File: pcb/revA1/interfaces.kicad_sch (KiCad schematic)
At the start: 18 parts, among them J2 Conn_02x30_Row_Letter_First, SW1 SW_DIP_x05, U22 SN74LV1T34DBV, U3 74AHCT1G125DB, U4 SN74CB3T3245PW, U5 SN74CB3T3245PW, U6 SN74CB3T3245PW, U7 SN74CB3T3245PW

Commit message: revA1, WIP
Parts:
- added BTN2: NMI, footprints:SW_SPST_PTS810_handsoldering, symbol Switch:SW_Push
- added C16: 100n, Capacitor_SMD:C_0603_1608Metric_Pad1.08x0.95mm_HandSolder, symbol Device:C
- added D17: L7, LED_SMD:LED_0603_1608Metric_Pad1.05x0.95mm_HandSolder, symbol Device:LED
- added J3: uSD card, footprints:Conn_uSDcard, symbol retro:MicroSD_Molex
- added JP2: Reverse, Jumper:SolderJumper-2_P1.3mm_Open_RoundedPad1.0x1.5mm, symbol Jumper:Jumper_2_Open
- added R14, R15, R50, R51: 10k, Resistor_SMD:R_0603_1608Metric_Pad0.98x0.95mm_HandSolder, symbol Device:R
- added R52: 1k, Resistor_SMD:R_0603_1608Metric_Pad0.98x0.95mm_HandSolder, symbol Device:R
- added U4: 74AHCT1G125DB, Package_TO_SOT_SMD:SOT-23-5_HandSoldering, symbol 74xGxx:74LVC1G125
- BTN1: value Reset -> RST
- renumbered R46 to R10, R10 to R11, R11 to R12, R12 to R13, U4 to U5, U5 to U6, U6 to U7, U7 to U8, U22 to U9
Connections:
- net +3V3: now also C16.1, J3.4 (VDD), R14.2, R15.2, R50.1, R52.1
- net +5V: now also R51.1, U4.2, U4.5 (VCC)
- net GND: now also BTN2.2, C16.2, J3.10 (CD2), J3.11 (SH), J3.12 (SH), J3.13 (SH), J3.14 (SH), J3.15 (SH), J3.6 (GND), JP2.1 (A), U4.3 (GND)
- net ~{IODOS}: no longer U7.17 (B1)
- net at J2.a25 (Pin_a25): now also U4.4
- net ~{NMI}: now reaches J2.b14 (Pin_b14)
- net ~{NMI}: now also U7.17 (B1), R51.2
- net +12V: no longer names the net of J2.b29 (Pin_b29)
- net ~{xIODOS} renamed ~{xNMI}
- new net: D17.2 (A), R52.2
- new net CFG5: JP2.2 (B)
- new net LED1: D17.1 (K)
- new net SD_CLK: J3.5 (SCLK)
- new net SD_DI: J3.3 (DI)
- new net SD_DO: J3.7 (DO)
- new net ~{BTN_NMI}: BTN2.1, R50.2
- new net ~{ROMCS}: U4.1
- new net ~{SD_CS}: J3.2 (~{CS}), R14.1
- new net ~{SD_DET}: J3.9 (CD1), R15.1
- no-connect marks 22 -> 21
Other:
- note added: "+12"
- note added: "+5"
- note added: "BLK"
- note added: "BUSACK"
- note added: "BUSREQ"
- note added: "CLK"
- note added: "F"
- note added: "HALT"
- note added: "INT"
- note added: "LED"
- note added: "MAGIC BUTTON"
- note added: "RDR"
- note added: "RFSH"
- note added: "RS"
- note added: "SD CARD"
- note added: "TURBO"
- moved on the sheet: U6, U8

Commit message: revA1
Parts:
- added D18: 1N4148W, Diode_SMD:D_SOD-123, symbol Diode:1N4148W
- added JP3: Audio L, Jumper:SolderJumper-2_P1.3mm_Open_RoundedPad1.0x1.5mm, symbol Jumper:Jumper_2_Open
- added JP4: Audio R, Jumper:SolderJumper-2_P1.3mm_Open_RoundedPad1.0x1.5mm, symbol Jumper:Jumper_2_Open
- added R53: 27, Resistor_SMD:R_0603_1608Metric_Pad0.98x0.95mm_HandSolder, symbol Device:R
- J2: value Conn_02x30_Row_Letter_First -> Conn_02x31_Row_Letter_First; footprint my:ZX_NEMO_60_EDGE -> my:ZX_NEMO_62_EDGE; symbol Connector_Generic:Conn_02x30_Row_Letter_First -> Connector_Generic:Conn_02x31_Row_Letter_First; now in the parts list
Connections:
- net ~{DOS}: no longer U6.15 (B3)
- net ~{RST}: now also R53.2
- net F: now reaches J2.a5 (Pin_a5)
- net F: now also U6.15 (B3)
- net ~{xDOS} renamed xF
- new net: J2.a31 (Pin_a31), JP3.2 (B)
- new net: J2.b31 (Pin_b31), JP4.1 (A)
- new net: D18.2 (A), R53.1
- new net SND_L: JP3.1 (A)
- new net SND_R: JP4.2 (B)
- new net ~{oRST}: D18.1 (K)
- no-connect marks 21 -> 20
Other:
- note added: "Reset output (active 0)"
- note removed: "F"
- moved on the sheet: U9

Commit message: Small improvements to the revA1
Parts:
- added J7: NMI, Connector_PinHeader_2.54mm:PinHeader_1x02_P2.54mm_Vertical, symbol Connector_Generic:Conn_01x02
- JP2: value Reverse -> VU Reverse
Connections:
- net GND: now also J7.2 (Pin_2)
- net ~{BTN_NMI}: now also J7.1 (Pin_1)
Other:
- moved on the sheet: BTN2, R50

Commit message: Fixed missing LED1 connection, new revA1 release
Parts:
- D17: value L7 -> RED
- J2, JP2, JP3, JP4: now left out of the parts list
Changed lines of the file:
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@@
 		(body_style 1)
 		(exclude_from_sim no)
-		(in_bom yes)
+		(in_bom no)
 		(on_board yes)
 		(in_pos_files yes)
@@
 		(body_style 1)
 		(exclude_from_sim no)
-		(in_bom yes)
+		(in_bom no)
 		(on_board yes)
 		(in_pos_files yes)
@@
 		(body_style 1)
 		(exclude_from_sim no)
-		(in_bom yes)
+		(in_bom no)
 		(on_board yes)
 		(in_pos_files yes)
@@
 			)
 		)
-		(property "Value" "L7"
+		(property "Value" "RED"
 			(at 254 147.066 0)
 			(show_name no)
@@
 		(body_style 1)
 		(exclude_from_sim no)
-		(in_bom yes)
+		(in_bom no)
 		(on_board yes)
 		(in_pos_files yes)

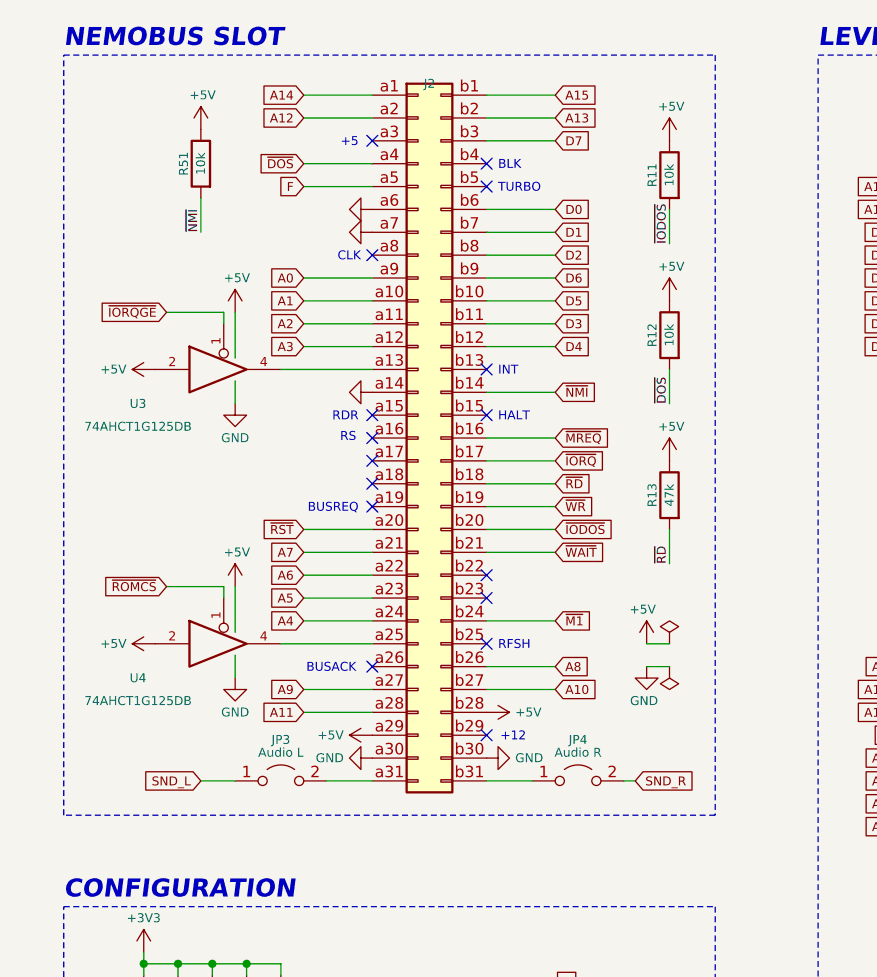
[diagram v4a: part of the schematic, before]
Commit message: Fixed ROM block signal: swapped CSR / RDR
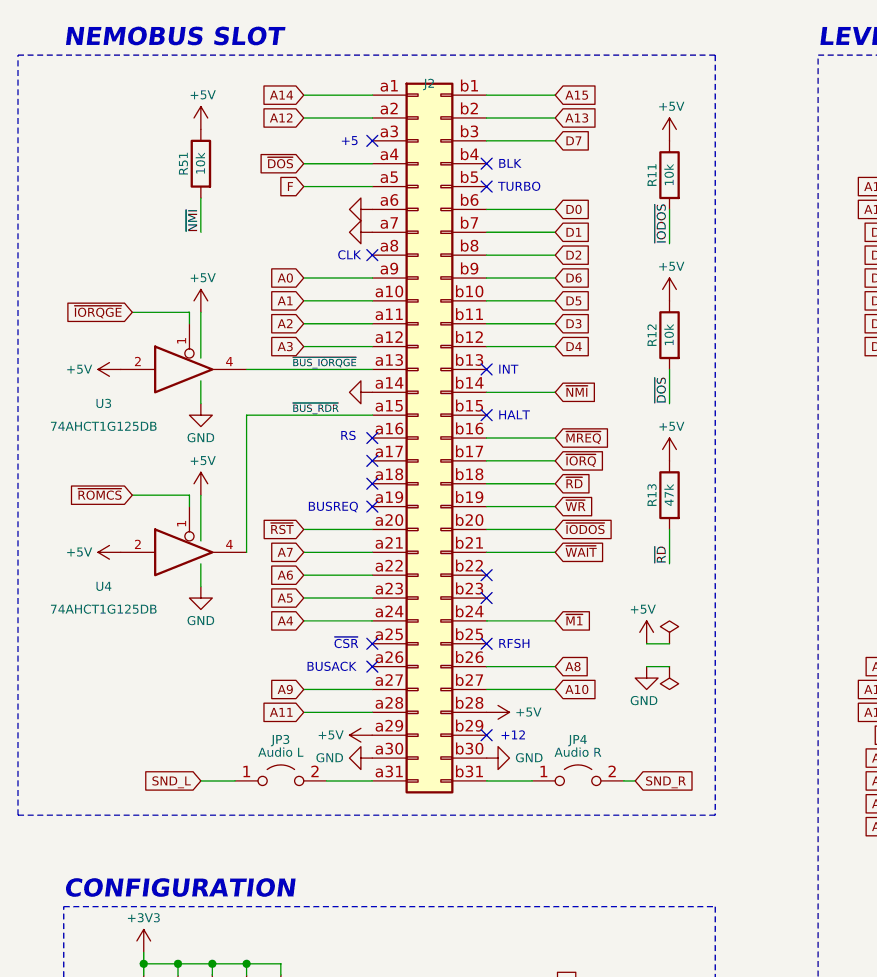
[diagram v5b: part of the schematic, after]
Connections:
- net ~{BUS_IORQGE}: now reaches J2.a13 (Pin_a13), U3.4
- net ~{BUS_RDR}: now reaches J2.a15 (Pin_a15)
- net ~{BUS_RDR}: now also U4.4
- net at J2.a25 (Pin_a25): no longer U4.4
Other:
- note added: "~{CSR}"
- note removed: "RDR"
- moved on the sheet: U3, U4

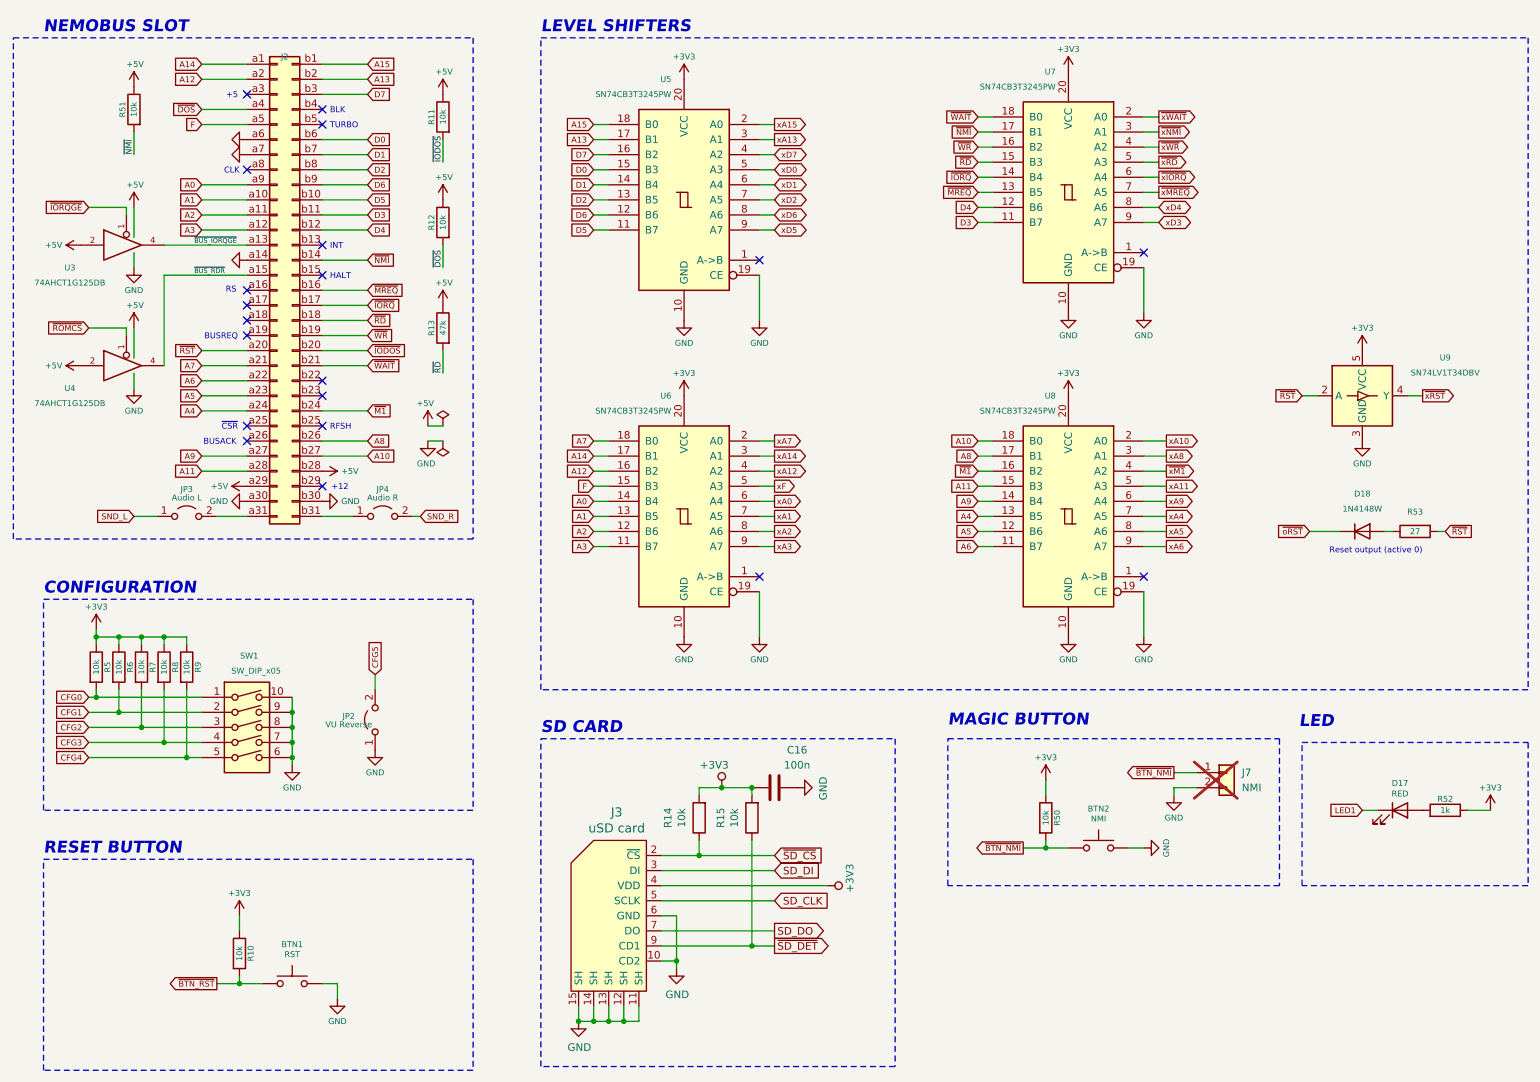
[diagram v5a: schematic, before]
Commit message: DivMMC + ZC for revA1 (#1)
* Current Divmmc WIP

* Added zx rom, fixed divmmc port decoding

* Fixed A1 Schematics / PCB with RDR + BLK signals

* Fixed divmmc by areset

* WIP

* Working 64kb divmmc + GS rom via flash loader

* removed zc_busy

* Project file update for 25k fpga

* Build files for 25k

* Fixed project for revA 16k

* Fixed project for revA 25k

* Added synth macros HW_A1

* Added synth macros HW_A1
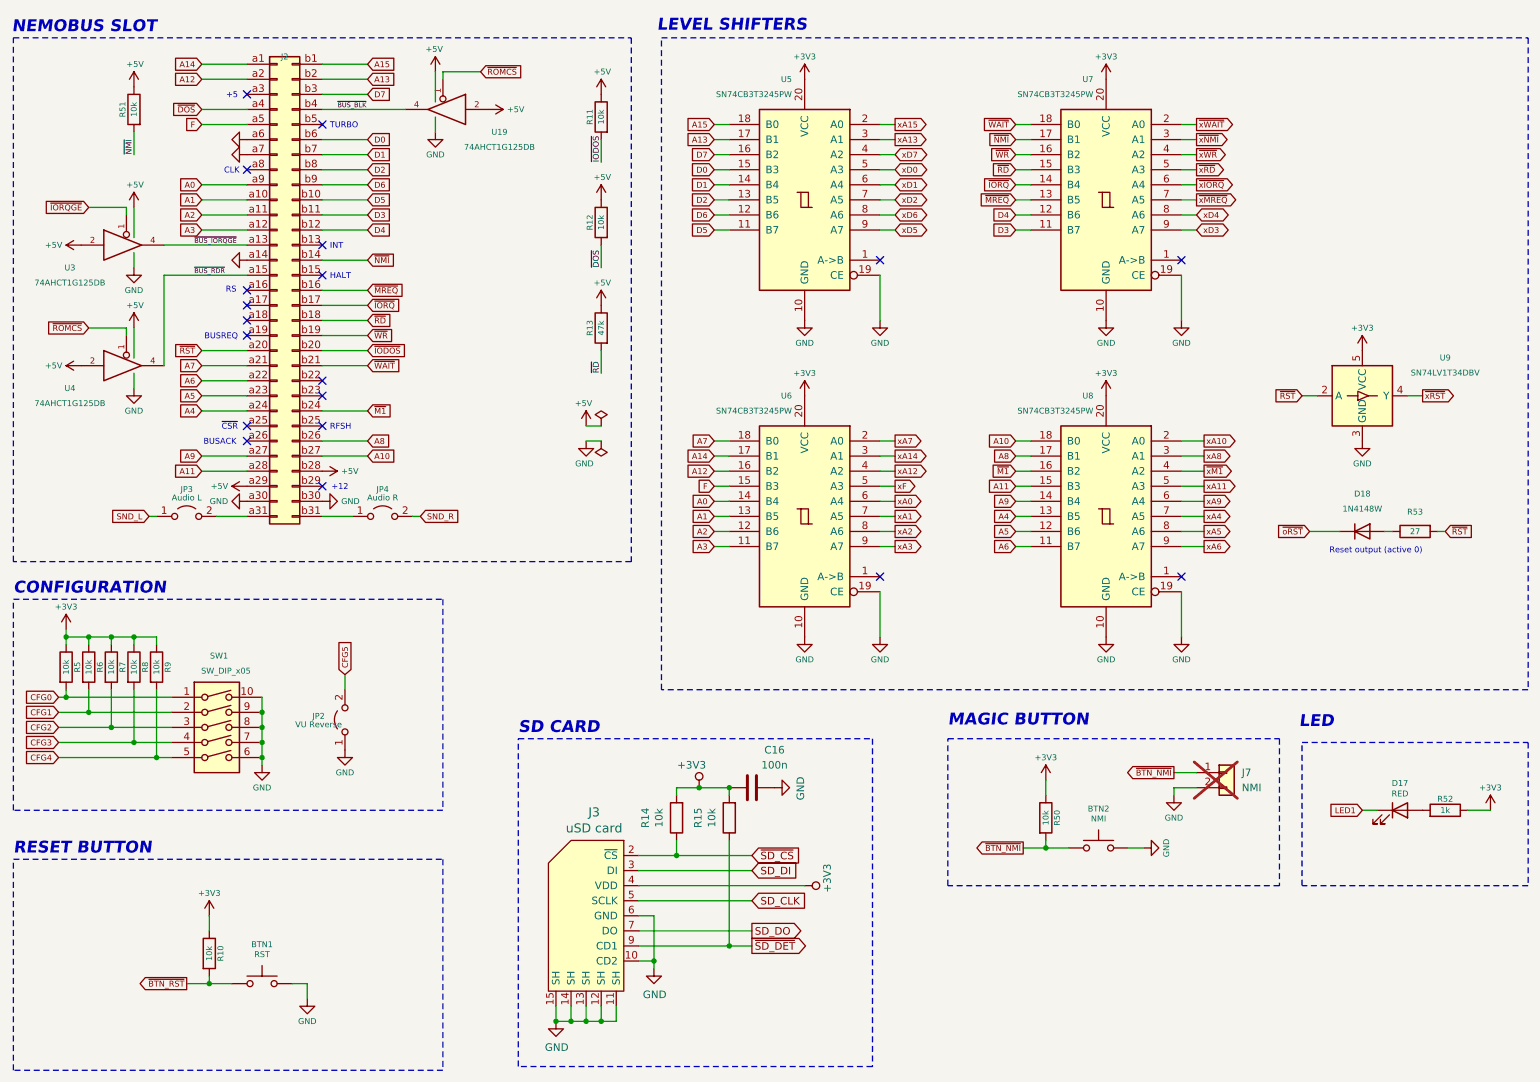
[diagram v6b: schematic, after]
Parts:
- added U19: 74AHCT1G125DB, Package_TO_SOT_SMD:SOT-23-5_HandSoldering, symbol 74xGxx:74LVC1G125
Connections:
- net +5V: now also U19.2, U19.5 (VCC)
- net GND: now also U19.3 (GND)
- net ~{ROMCS}: now also U19.1
- net ~{BUS_BLK}: now reaches J2.b4 (Pin_b4)
- net ~{BUS_BLK}: now also U19.4
- no-connect marks 20 -> 19
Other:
- note removed: "BLK"
- moved on the sheet: BTN1, C16, J3, JP2, R10, R11, R12, R13, R14, R15, R5, R6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
